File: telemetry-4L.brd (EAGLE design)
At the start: 69.8 x 22.9 mm, 74 parts, among them SW1 MF-SW-TACT-4.2MM, SW2 PCM12SMTR, U1 ATSAMD21G18A-MUT, U2 SPX3819M5-L-3-0, U3 MCP73831T-2ACI/OT, U4 IRLML6344TRPBF, U5 SIM868, U6 BMP280, U7 MPU-9250, U8 TPS61253YFFR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

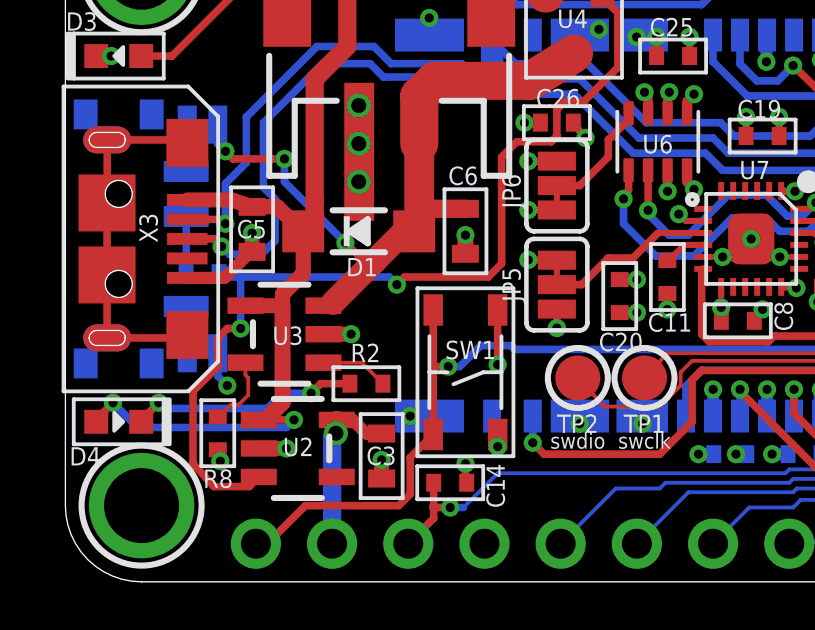
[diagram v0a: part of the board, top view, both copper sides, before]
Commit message: Fixed a problem with overlapping diode and cleaned up files
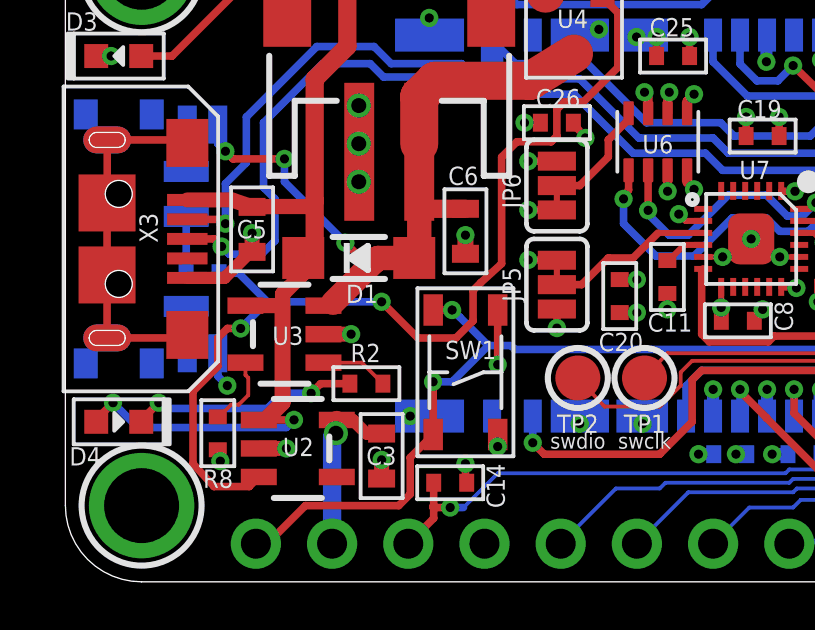
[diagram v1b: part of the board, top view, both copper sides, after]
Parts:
- moved D1 0.89 mm to (9.78, 10.8)
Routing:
- net EN: track 34.0 -> 35.6 mm
- net VBAT: track 23.8 -> 24.3 mm
- net !RESET: track 35.8 -> 35.9 mm, vias 2 -> 3

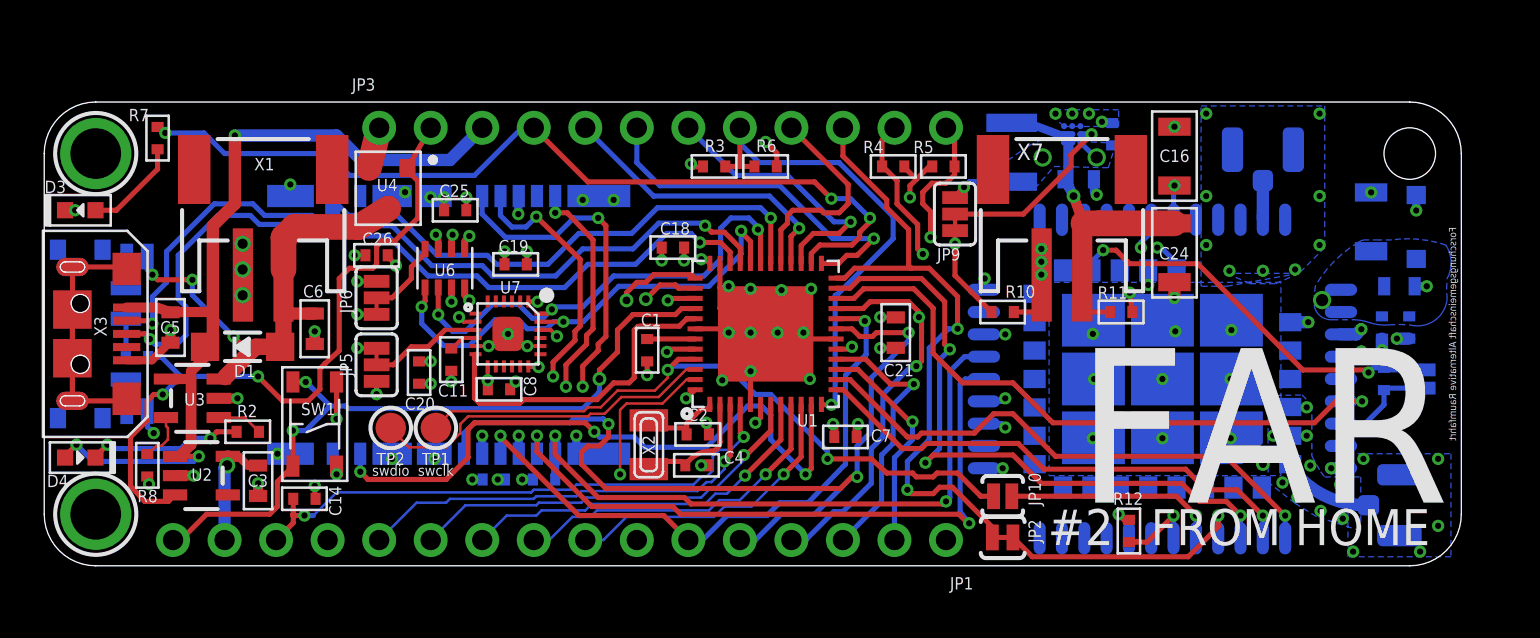
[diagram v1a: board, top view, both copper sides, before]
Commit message: More fixes of overlapping components
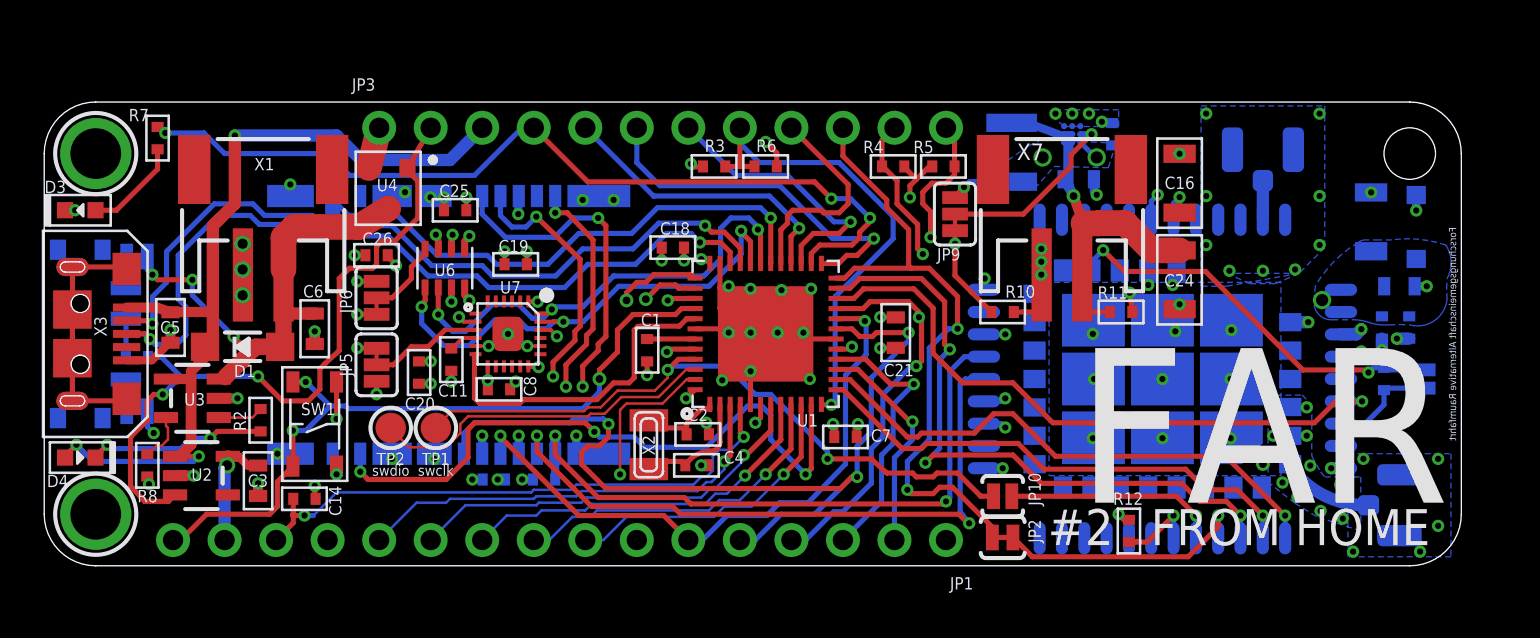
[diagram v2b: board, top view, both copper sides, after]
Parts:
- moved C16 1.36 mm to (56.0, 18.9)
- moved C24 1.36 mm to (56.0, 14.1)
- moved R2 0.85 mm to (10.7, 7.18), turned to 90 degrees
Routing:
- net TX5/GPS_RX: track 37.4 -> 34.8 mm
- net N$1: track 7.67 -> 8.86 mm
- net GND: track 85.7 -> 85.0 mm

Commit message: Connected 1PPS via jumper made CTS jumper default NO
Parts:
- added JP11: JUMPER-PAD-2-NOYES_SILK, SparkFun-Passives:PAD-JUMPER-2-NO_YES_SILK
- JP2: value JUMPER-PAD-2-NC_BY_TRACE -> JUMPER-PAD-2-NOYES_SILK; device SparkFun-Passives:PAD-JUMPER-2-NC_BY_TRACE_YES_SILK -> SparkFun-Passives:PAD-JUMPER-2-NO_YES_SILK
- moved C7 0.19 mm to (39.5, 6.54)
- moved C21 0.06 mm to (42.0, 11.5)
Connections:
- net GPS_1PPS: now also JP11.2
- net SWDIO: now also JP11.1
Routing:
- net SWDIO: track 17.3 -> 35.9 mm, vias 0 -> 2
- net GPS_1PPS: track 0.00 -> 17.5 mm, vias 0 -> 3
- net MISO: track 55.4 -> 51.3 mm, vias 4 -> 3
- net MOSI: track 44.8 -> 41.9 mm
- net D1/TX0: track 11.0 -> 12.9 mm
- net STATUS: track 42.0 -> 40.4 mm
- net D4/TX2/GSM_RX: track 24.9 -> 26.4 mm
- net D5/CTS2: track 31.6 -> 30.5 mm
- net D0/RX0: track 13.5 -> 14.5 mm
- net D8/SD_CS: track 32.0 -> 32.9 mm
- net SCK: track 30.6 -> 31.5 mm
- net D3/RX2/GSM_TX: track 27.0 -> 27.8 mm
- net SWCLK: track 33.6 -> 34.3 mm
- net PWRKEY: track 31.6 -> 31.0 mm
- net RTS2: track 32.6 -> 32.1 mm

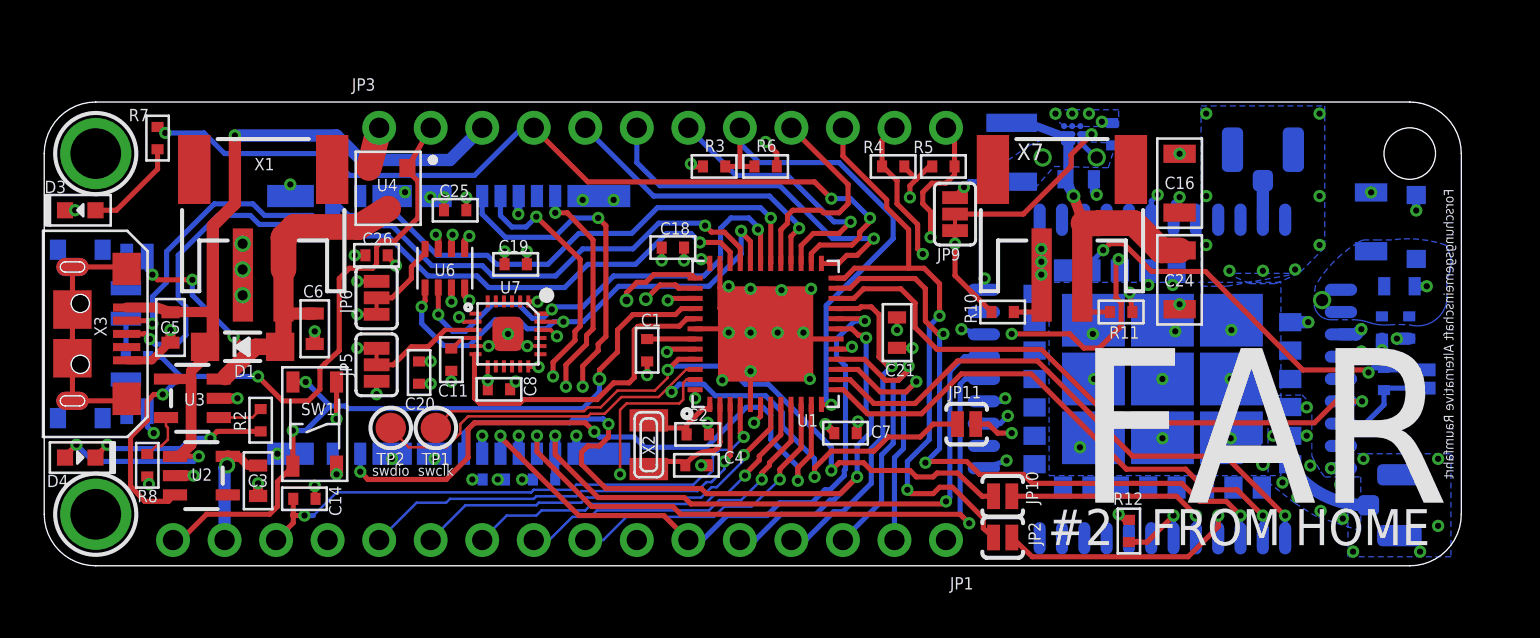
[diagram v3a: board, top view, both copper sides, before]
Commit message: Increased margins in middle part of board
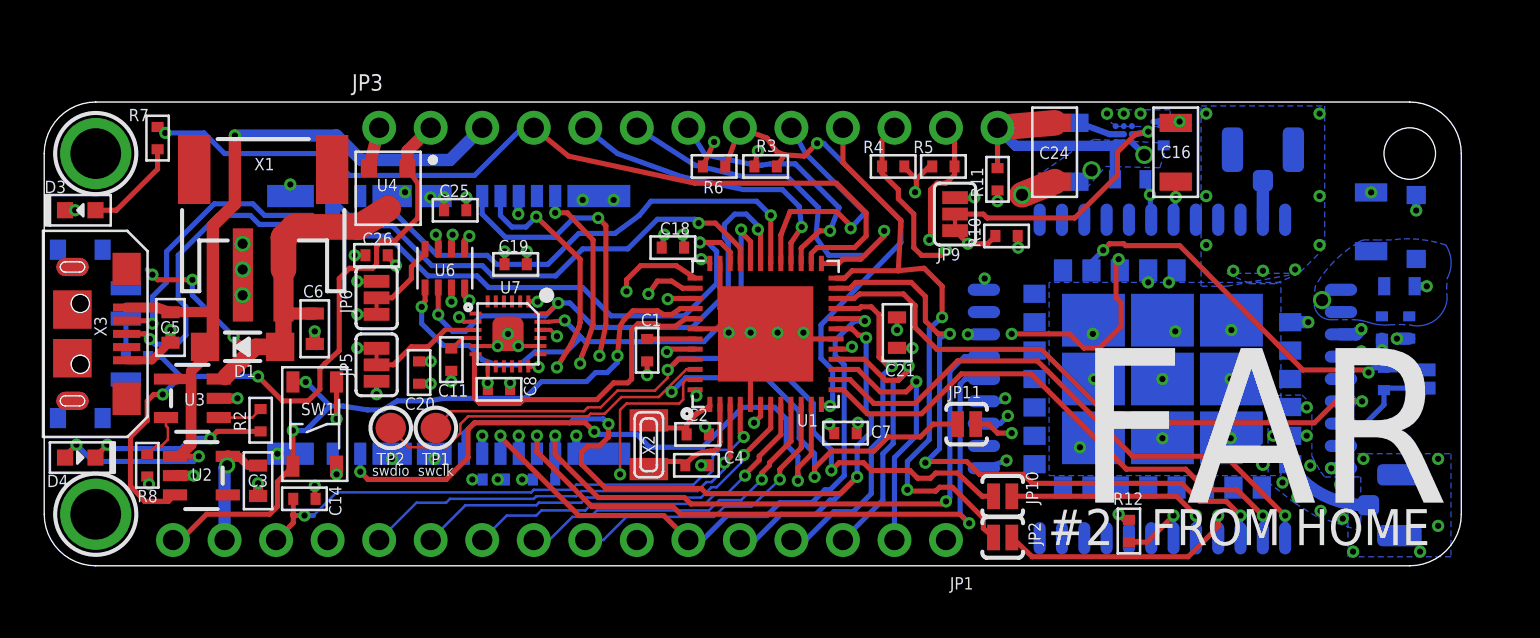
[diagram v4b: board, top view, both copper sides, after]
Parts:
- removed JP7, JP8: JUMPER-PAD-2-NC_BY_TRACE, SparkFun-Passives:PAD-JUMPER-2-NC_BY_TRACE_YES_SILK
- removed X7: S2B-PH-SM4-TB(LF)(SN), microbuilder:JSTPH2
- JP3: device microbuilder:1X12_ROUND -> microbuilder:1X13_ROUND_70
- R1: value 100K -> 10K
- moved R11 8.94 mm to (47.0, 19.1), turned to 270 degrees
- moved C24 8.80 mm to (49.8, 20.4)
- moved R10 3.75 mm to (47.4, 16.3)
- moved C23 2.54 mm to (53.5, 19.1)
- moved C22 2.54 mm to (55.2, 21.3)
- moved L1 2.54 mm to (50.2, 20.4)
- moved R3 2.54 mm to (35.6, 19.7)
- moved R6 2.54 mm to (33.0, 19.7), turned to 180 degrees
- moved U8 2.54 mm to (53.2, 21.3)
- moved C16 1.54 mm to (55.8, 20.4)
- moved JP3 1.27 mm to (31.8, 21.6)
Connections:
- removed net N$12: JP7.2, SW2.O
- removed net N$13: JP8.2, SW2.S
- removed net SLD: X3.S1, X3.S2, X3.S3, X3.S4, X3.S5, X3.S6
- net 5.0V: now also JP3.13; no longer X7.2
- net GND: now also SW2.O, X3.S1, X3.S2, X3.S3, X3.S4, X3.S5, X3.S6; no longer JP7.1, X7.1
- net VBAT: now also SW2.S; no longer JP8.1
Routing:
- net +3V: track 33.8 -> 70.7 mm
- net SLD: track 12.0 -> 0.00 mm
- net SCL: track 42.6 -> 46.8 mm
- net MISO: track 51.3 -> 47.6 mm
- net 5V_EN: track 9.25 -> 12.8 mm
- net D+: track 39.0 -> 42.3 mm
- net 5.0V: track 16.2 -> 13.5 mm, vias 1 -> 0
- net VBAT_ON: track 58.1 -> 60.6 mm
- net D11: track 18.0 -> 20.0 mm
- net D6: track 10.7 -> 12.6 mm, vias 0 -> 1
- net SERVO_EN: track 21.7 -> 20.0 mm
- net SIM_CLK: track 37.2 -> 35.6 mm
- net N$13: track 1.57 -> 0.00 mm
- net N$12: track 1.57 -> 0.00 mm
- net SWCLK: track 34.3 -> 35.5 mm
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
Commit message: Improvements on the right side
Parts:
- moved C22 0.89 mm to (56.1, 21.3)
- moved U8 0.44 mm to (53.7, 21.3)
- moved C23 0.37 mm to (53.8, 18.9)
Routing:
- net GPS_1PPS: track 17.5 -> 18.2 mm
- net GPS_EN_: track 19.9 -> 20.6 mm
- net GND: track 85.3 -> 85.1 mm, vias 106 -> 107

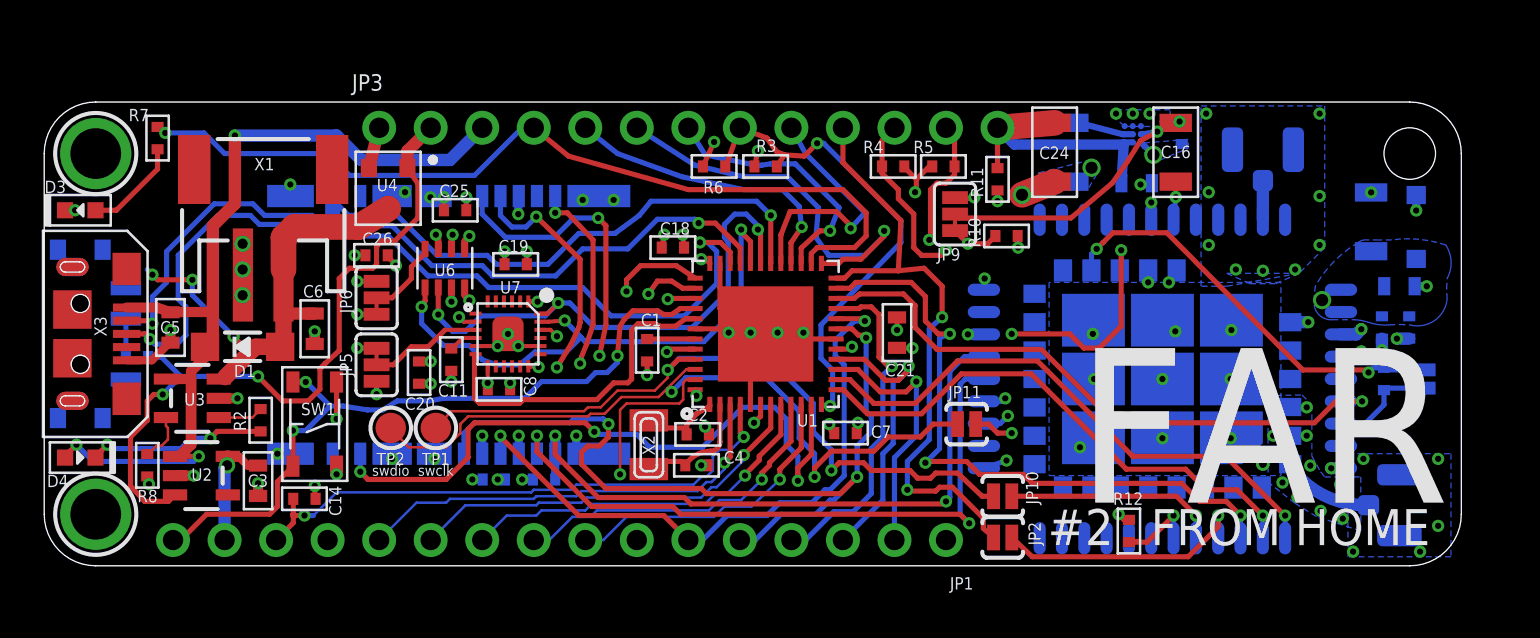
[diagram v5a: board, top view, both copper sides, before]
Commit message: Fixed bigger margins on the right side¨ Only left side remains
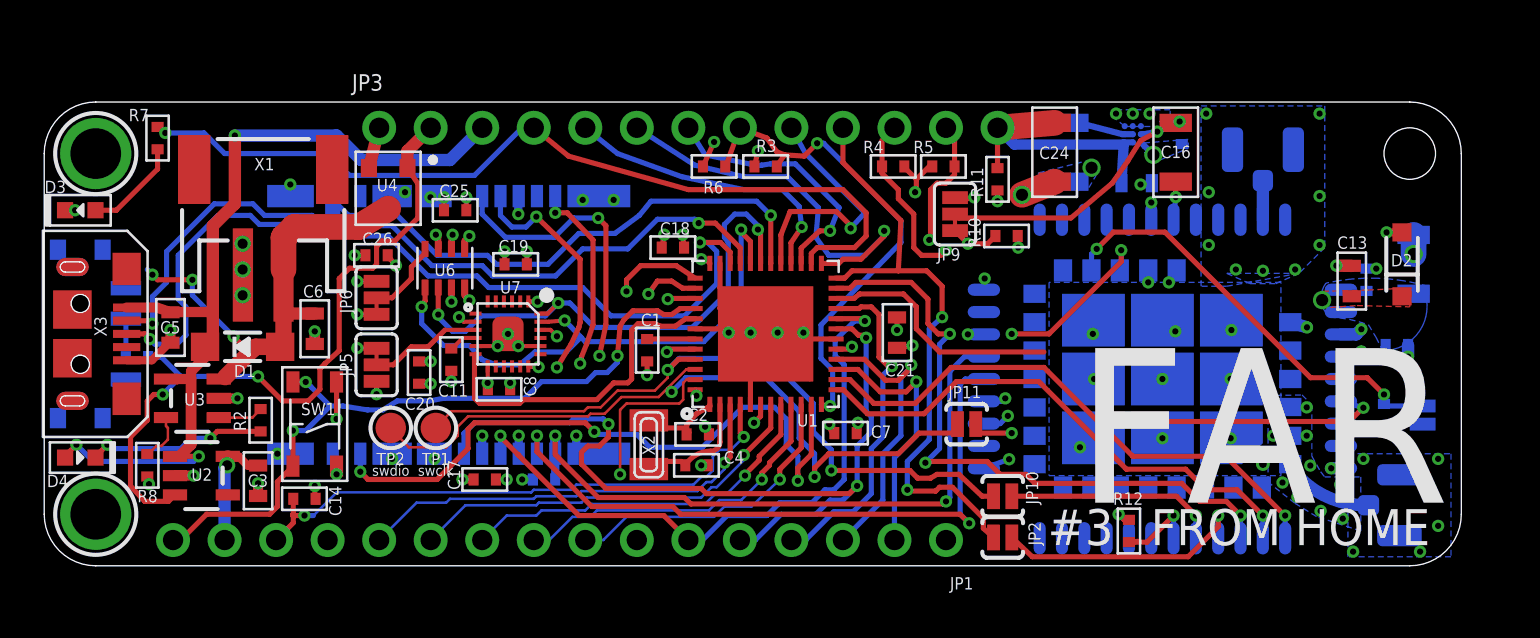
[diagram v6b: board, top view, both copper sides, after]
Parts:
- moved C12 3.16 mm to (65.2, 14.1), turned to 90 degrees
- moved C15 2.96 mm to (67.5, 14.9)
- moved C13 2.36 mm to (64.5, 14.0), flipped to the top, turned to 90 degrees
- moved D2 1.97 mm to (66.9, 14.9), flipped to the top
- moved JP4 1.78 mm to (67.9, 7.43)
- moved R9 1.78 mm to (66.0, 7.43)
- moved C10 1.14 mm to (66.7, 10.9), turned to 180 degrees
- moved C17 0.44 mm to (21.7, 4.25), flipped to the top, turned to 0 degrees
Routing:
- net +3V: track 70.7 -> 83.1 mm
- net PWRKEY: track 30.7 -> 25.9 mm
- net GPS_1PPS: track 18.2 -> 16.1 mm
- net GND: track 85.1 -> 86.4 mm
- net VDD_EXT_2V8: track 5.17 -> 4.20 mm
- net GPS_EN_: track 20.6 -> 21.4 mm
- added copper zone on layer 1, net VBAT_ON
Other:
- board text added: "#3"
- board text removed: "#2"

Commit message: Misc improvements
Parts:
- moved TP2 18.8 mm to (35.6, 10.3), flipped to the bottom
- moved TP1 17.3 mm to (35.6, 12.6), flipped to the bottom
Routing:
- net SWDIO: track 36.9 -> 23.4 mm
- net GND: track 86.4 -> 77.3 mm, vias 107 -> 105
- net SWCLK: track 35.1 -> 26.4 mm
- net +3V: track 83.1 -> 80.8 mm
- net MPU_INT: track 16.8 -> 15.5 mm
- net SIM_DATA: track 39.7 -> 38.6 mm
- net SIM_CLK: track 35.6 -> 34.6 mm
- net STATUS: track 39.8 -> 40.8 mm
- net SDA: track 41.2 -> 40.3 mm
- net D+: track 42.3 -> 41.5 mm
- net SCL: track 46.8 -> 46.0 mm
- net MOSI: track 42.0 -> 41.2 mm
- net TX5/GPS_RX: track 35.6 -> 35.0 mm
